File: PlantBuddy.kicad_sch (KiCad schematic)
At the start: 39 parts, among them J1 USB_C_Receptacle_USB2.0, J2 C+, J3 C-, J4 Expansion Header, SW1 SW_Push, U1 LTR-303ALS-01, U2 SHTC3, U3 ESP32-S3-WROOM-1-N8R8, U4 BQ24072RGT, U5 RT9080-33GJ5

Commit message: Silkscreen & testpoints
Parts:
- added TP1, TP2, TP3: TestPoint, TestPoint:TestPoint_Pad_D2.0mm, symbol Connector:TestPoint
- BT1: LCSC (none) -> C189700; Link https://ro.farnell.com/multicomp/bc-2404/retainer-clip-24mm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 -> (none); MPN BC-2404 -> 532610271
- R11: value 1R -> 100m; LCSC C22936 -> C247025; MPN 0603WAF100KT5E -> 0603WAJ010KT5E
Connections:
- net +3V3: now also TP1.1
- net GND: now also TP2.1
- net csense: now also TP3.1
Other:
- note added: "touch14 ADC2_CH3"
- note removed: "touch14"
- moved on the sheet: C5, C6, J2, J3, R10, R11, R5, R6, R9, U4

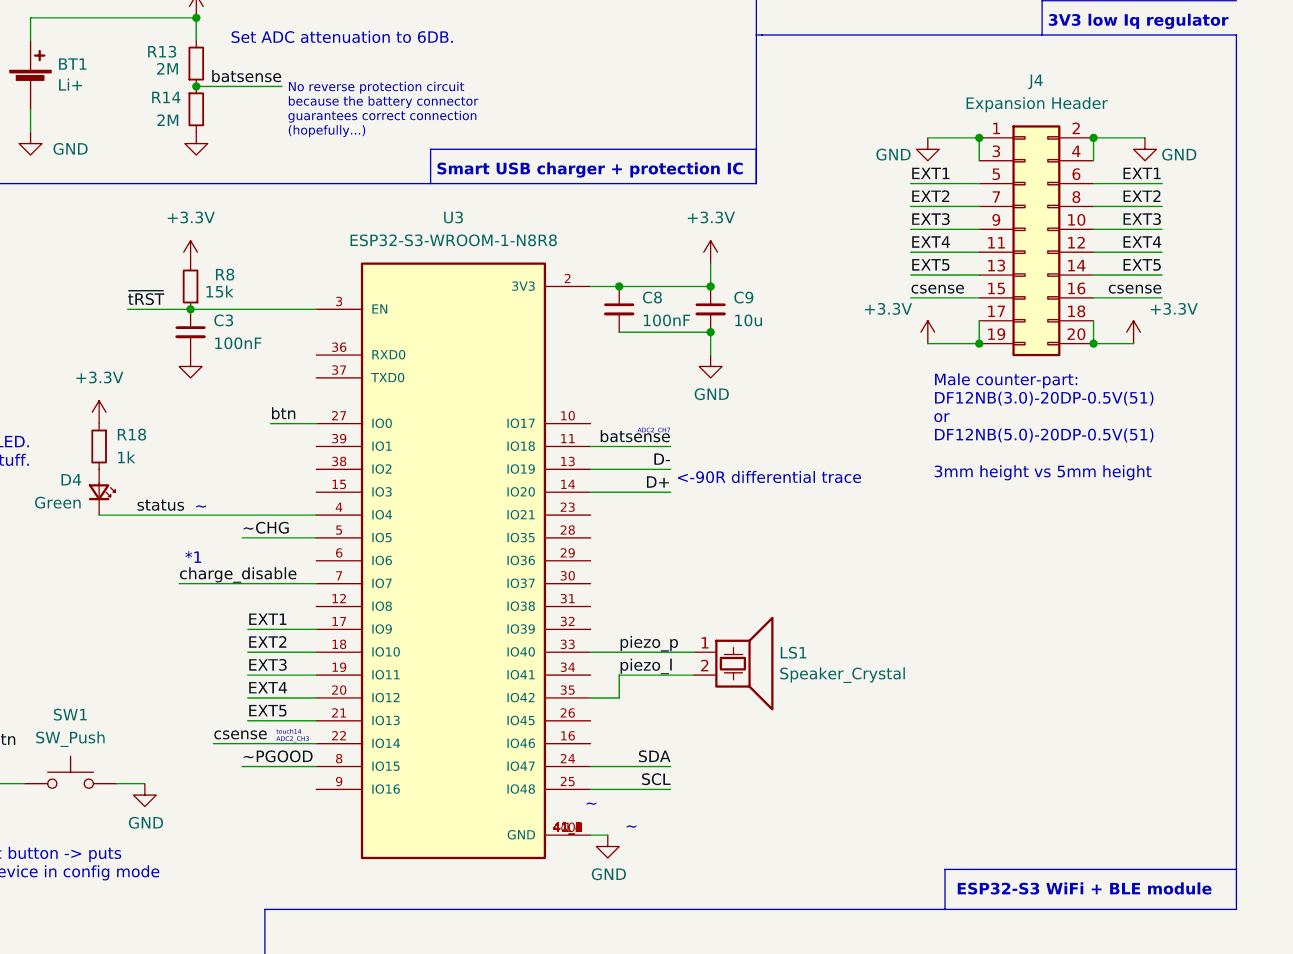
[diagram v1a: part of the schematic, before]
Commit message: Changed pin layout to have more EXT pins
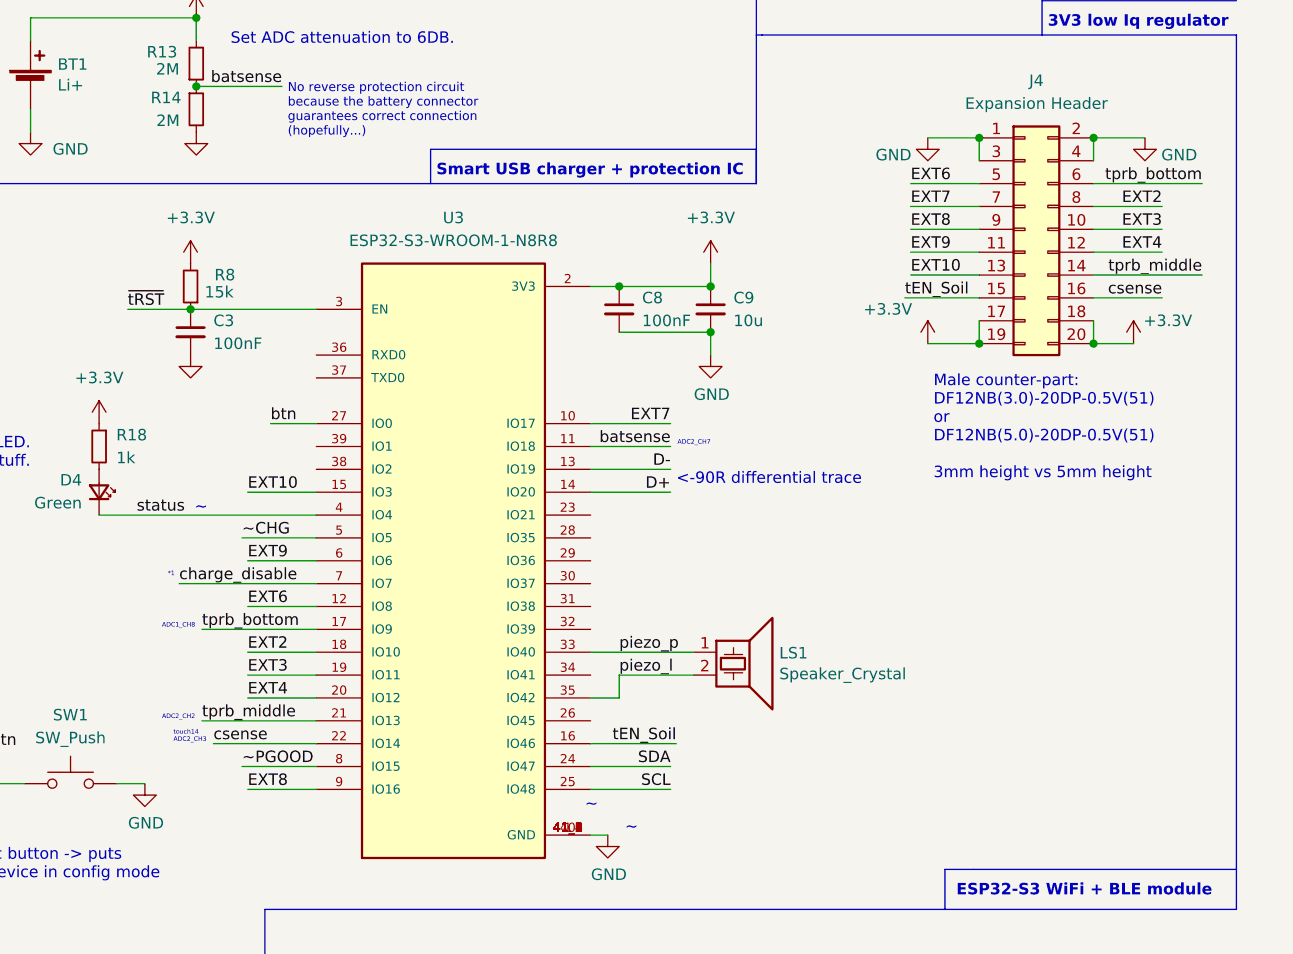
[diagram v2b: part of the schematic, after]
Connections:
- net EXT2: no longer J4.7 (Pin_7)
- net EXT3: no longer J4.9 (Pin_9)
- net EXT4: no longer J4.11 (Pin_11)
- net csense: no longer J4.15 (Pin_15)
- net EXT7: now reaches U3.10 (IO17)
- net EXT7: now also J4.7 (Pin_7)
- net EXT6: now reaches U3.12 (IO8)
- net EXT6: now also J4.5 (Pin_5)
- net EXT10: now reaches U3.15 (IO3)
- net EXT10: now also J4.13 (Pin_13)
- net tEN_Soil: now reaches U3.16 (IO46)
- net tEN_Soil: now also J4.15 (Pin_15)
- net EXT9: now reaches U3.6 (IO6)
- net EXT9: now also J4.11 (Pin_11)
- net EXT8: now reaches U3.9 (IO16)
- net EXT8: now also J4.9 (Pin_9)
- net EXT1 renamed tprb_bottom
- net tprb_bottom: no longer J4.5 (Pin_5)
- net EXT5 renamed tprb_middle
- net tprb_middle: no longer J4.13 (Pin_13)
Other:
- note added: "ADC1_CH8"
- note added: "ADC2_CH2"

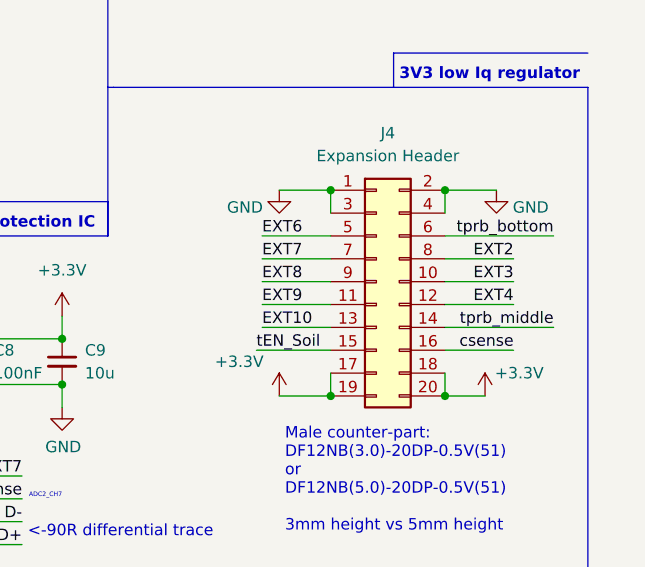
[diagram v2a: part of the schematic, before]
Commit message: Added different mezzannine connector
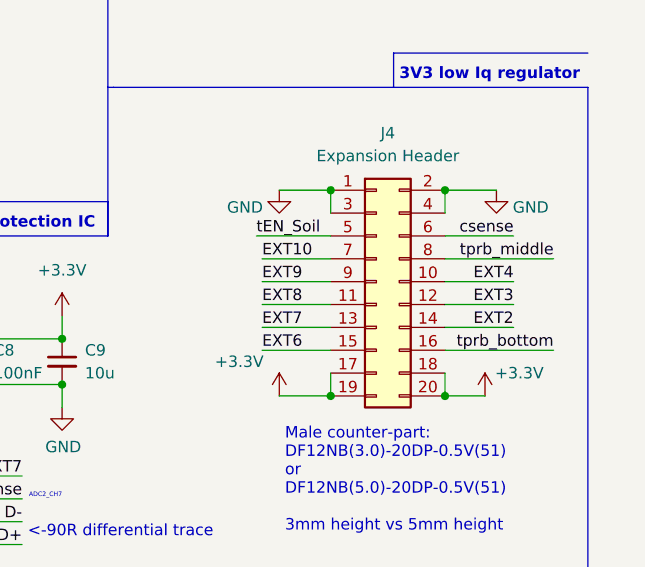
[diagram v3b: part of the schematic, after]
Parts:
- J4: footprint Mezzanine-pb:HRS_DF12NB-20DS-0.5V(51) -> Mezzanine-pb:HRS_BM20B(0.8)-20DS-0.4V(51); LCSC C2904117 -> C424535; MPN DF12NB-20DS-0.5V(51) -> BM20B(0.8)-20DS-0.4V(51)
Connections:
- net EXT10: now also J4.7 (Pin_7); no longer J4.13 (Pin_13)
- net EXT2: now also J4.14 (Pin_14); no longer J4.8 (Pin_8)
- net EXT3: now also J4.12 (Pin_12); no longer J4.10 (Pin_10)
- net EXT4: now also J4.10 (Pin_10); no longer J4.12 (Pin_12)
- net EXT6: now also J4.15 (Pin_15); no longer J4.5 (Pin_5)
- net EXT7: now also J4.13 (Pin_13); no longer J4.7 (Pin_7)
- net EXT8: now also J4.11 (Pin_11); no longer J4.9 (Pin_9)
- net EXT9: now also J4.9 (Pin_9); no longer J4.11 (Pin_11)
- net csense: now also J4.6 (Pin_6); no longer J4.16 (Pin_16)
- net tEN_Soil: now also J4.5 (Pin_5); no longer J4.15 (Pin_15)
- net tprb_bottom: now also J4.16 (Pin_16); no longer J4.6 (Pin_6)
- net tprb_middle: now also J4.8 (Pin_8); no longer J4.14 (Pin_14)

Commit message: Changed connector to a more solid one.
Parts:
- J4: footprint Mezzanine-pb:HRS_BM20B(0.8)-20DS-0.4V(51) -> Mezzanine-pb:AXK5F20547YG; LCSC C424535 -> C2917018; MPN BM20B(0.8)-20DS-0.4V(51) -> AXK5F20547YG
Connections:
- net EXT10: now also J4.13 (Pin_13); no longer J4.7 (Pin_7)
- net EXT2: now also J4.8 (Pin_8); no longer J4.14 (Pin_14)
- net EXT3: now also J4.10 (Pin_10); no longer J4.12 (Pin_12)
- net EXT4: now also J4.12 (Pin_12); no longer J4.10 (Pin_10)
- net EXT6: now also J4.5 (Pin_5); no longer J4.15 (Pin_15)
- net EXT7: now also J4.7 (Pin_7); no longer J4.13 (Pin_13)
- net EXT8: now also J4.9 (Pin_9); no longer J4.11 (Pin_11)
- net EXT9: now also J4.11 (Pin_11); no longer J4.9 (Pin_9)
- net csense: now also J4.16 (Pin_16); no longer J4.6 (Pin_6)
- net status: now also U3.23 (IO21); no longer U3.4 (IO4)
- net tEN_Soil: now also J4.15 (Pin_15); no longer J4.5 (Pin_5)
- net tprb_bottom: now also J4.6 (Pin_6); no longer J4.16 (Pin_16)
- net tprb_middle: now also J4.14 (Pin_14); no longer J4.8 (Pin_8)
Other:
- note added: "Male counter-part: AXK6F20347YG - 1.5mm or AXK6F20547YG - 2mm"
- note removed: "Male counter-part: DF12NB(3.0)-20DP-0.5V(51) or DF12NB(5.0)-20DP-0.5V(51) 3mm height vs 5mm height"

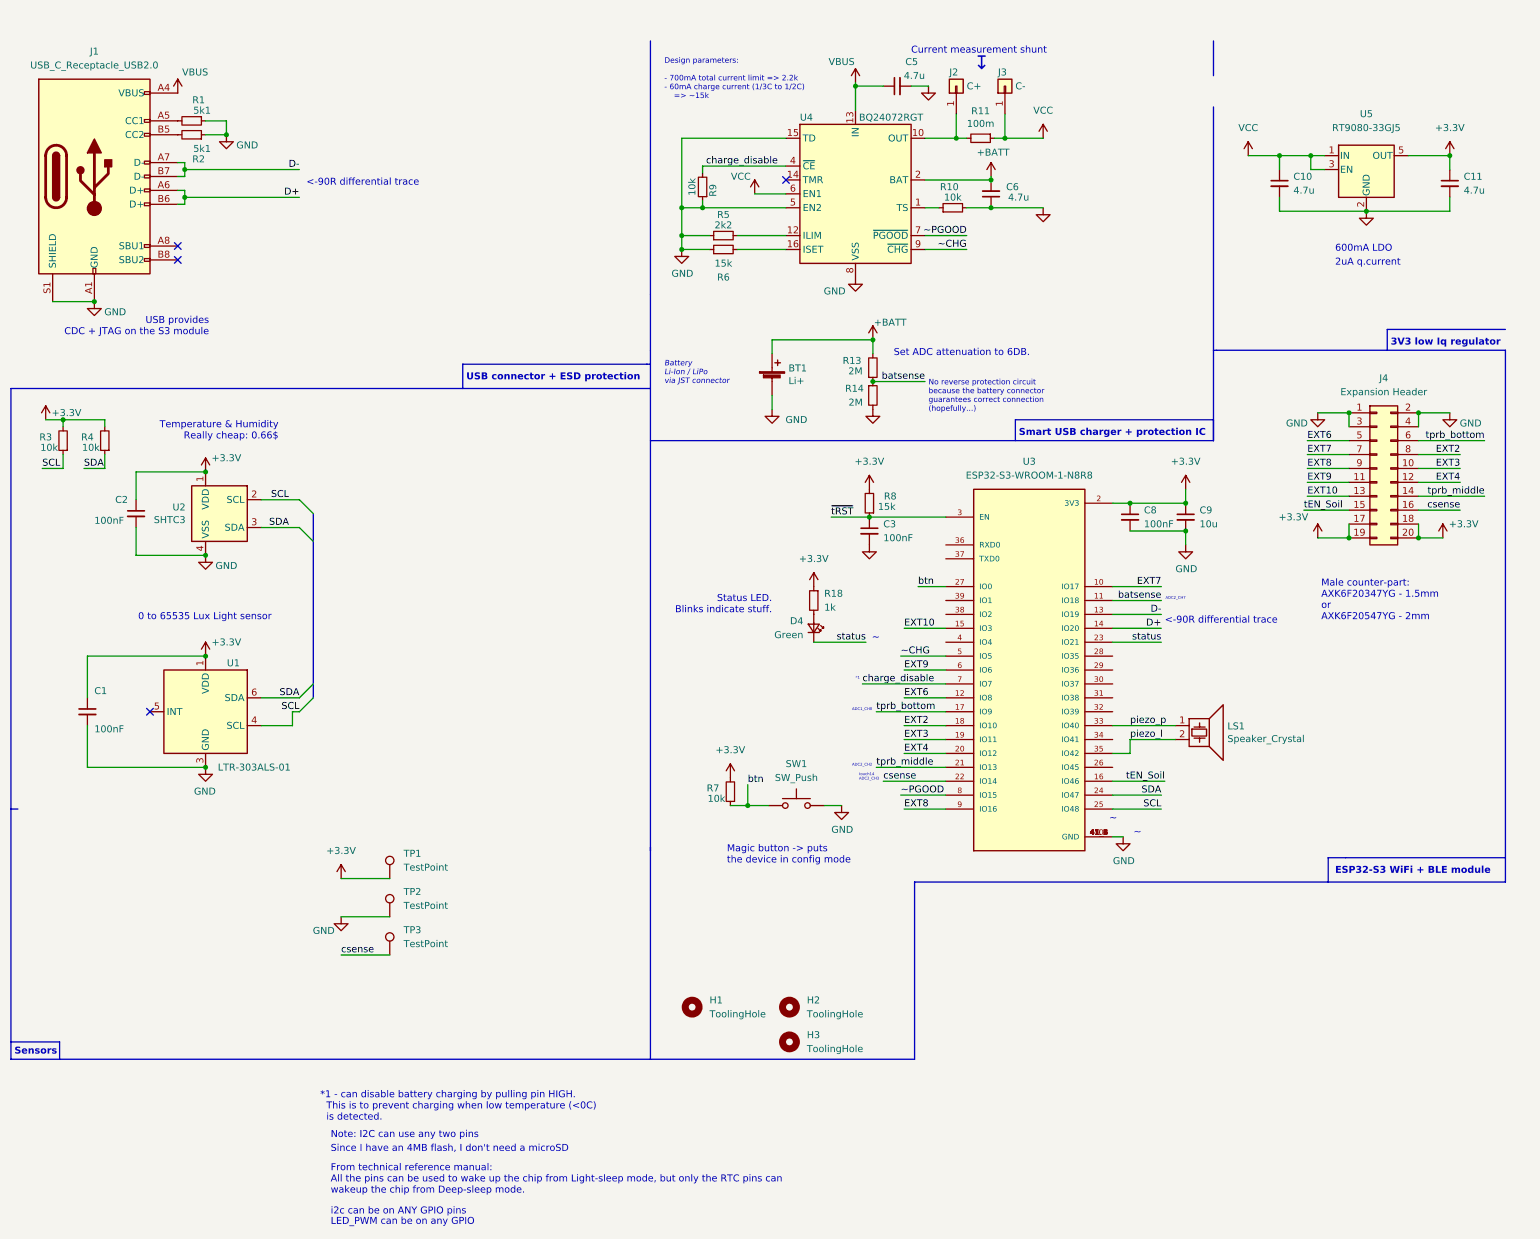
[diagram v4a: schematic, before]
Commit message: Converted to proper 4-layer and ordered PCB
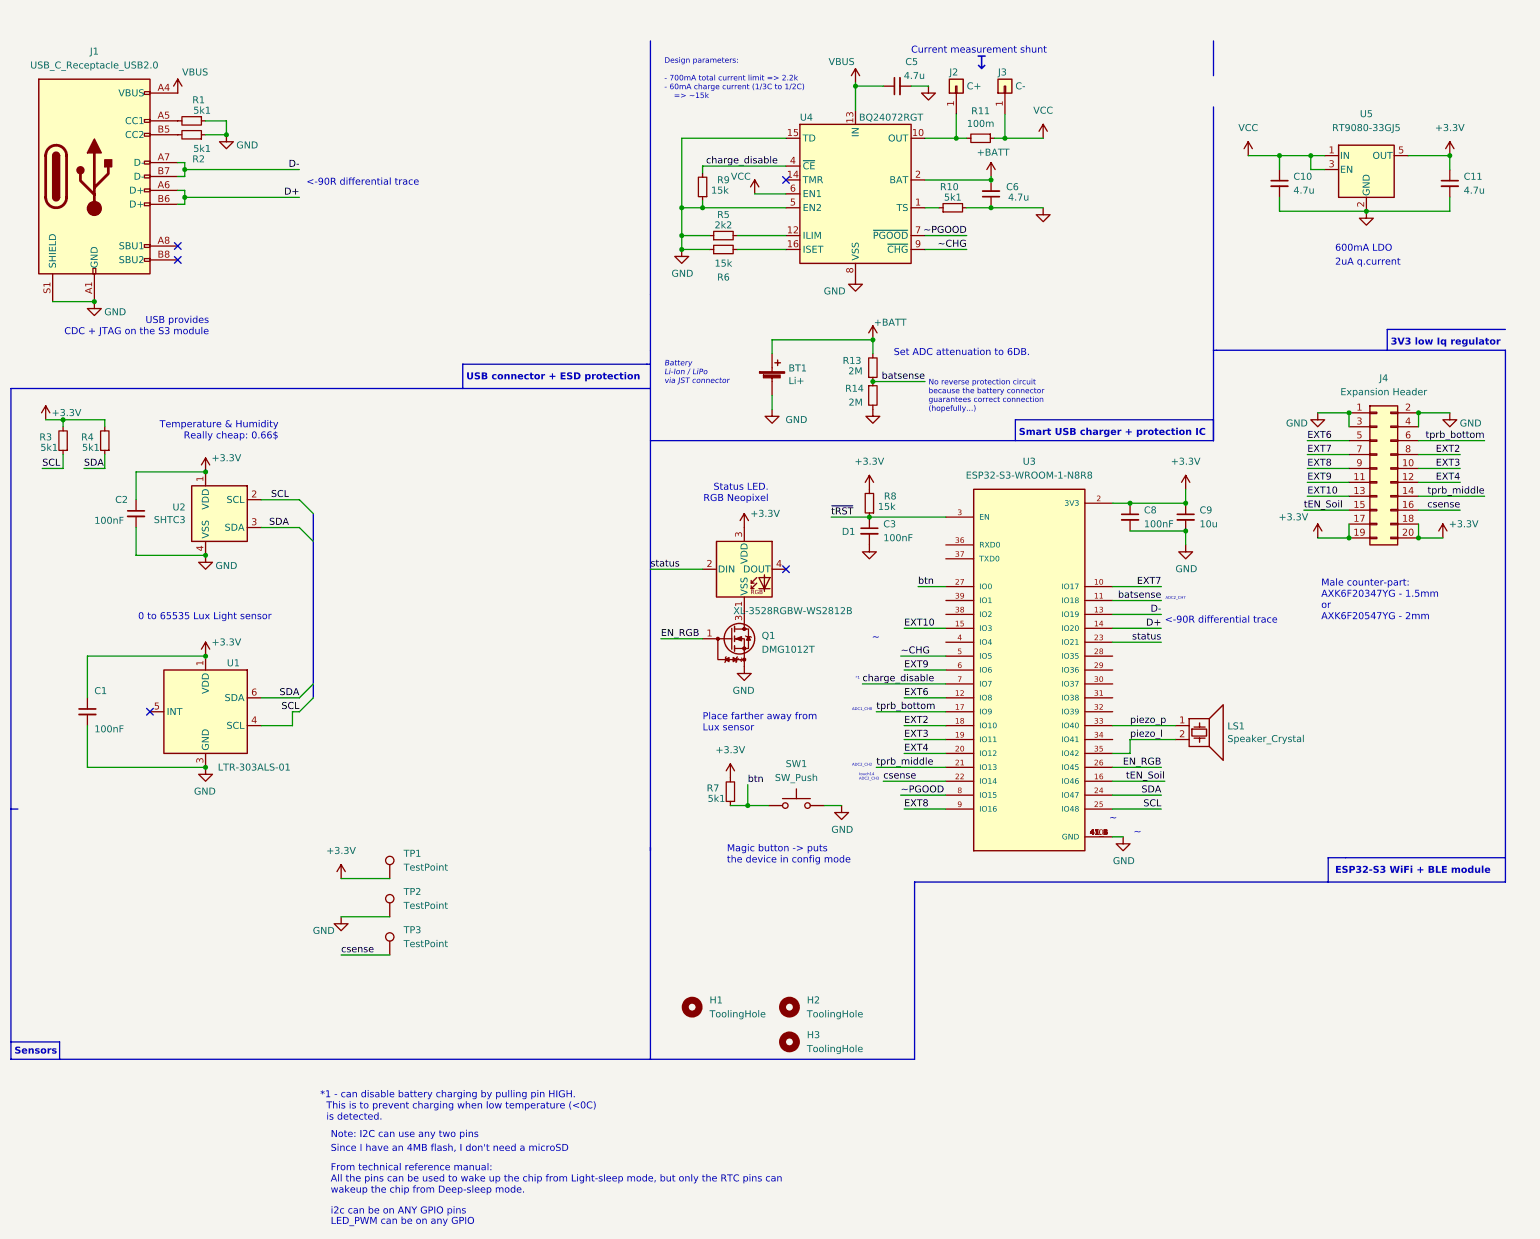
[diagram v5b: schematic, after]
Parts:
- removed D4: Green, LED_SMD:LED_0603_1608Metric, symbol Device:LED_Small
- removed R18: 1k, Resistor_SMD:R_0603_1608Metric, symbol Device:R_Small
- added D1: XL-3528RGBW-WS2812B, Neopixel:XL-3528RGBW-WS2812B, symbol neopixel:XL-3528RGBW-WS2812B
- added Q1: DMG1012T, Package_TO_SOT_SMD:SOT-523, symbol Transistor_FET:DMG1012T
- R10, R3, R4, R7: value 10k -> 5k1; LCSC C25804 -> C23186; MPN 0603WAF1002T5E -> 0603WAF5101T5E
- R9: value 10k -> 15k; LCSC C25804 -> C22809; MPN 0603WAF1002T5E -> 0603WAF1502T5E
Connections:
- net +3V3: now also D1.3 (VDD)
- net GND: now also Q1.2 (S)
- net status: now also D1.2 (DIN)
- net EN_RGB: now reaches U3.26 (IO45)
- net EN_RGB: now also Q1.1 (G)
- new net: D1.1 (VSS), Q1.3 (D)
- no-connect marks 4 -> 5
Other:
- note added: "Place farther away from Lux sensor"
- note added: "Status LED. RGB Neopixel"
- note removed: "Status LED. Blinks indicate stuff."
